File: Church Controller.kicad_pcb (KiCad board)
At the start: 2 copper layers, 50 x 90 mm, 26 parts, among them J1 Battery Connector, J2 Programming, J3 Prog Jumper, SW1 Change, SW2 Save, U1 AZ1117-3.3, U2 ESP-12E

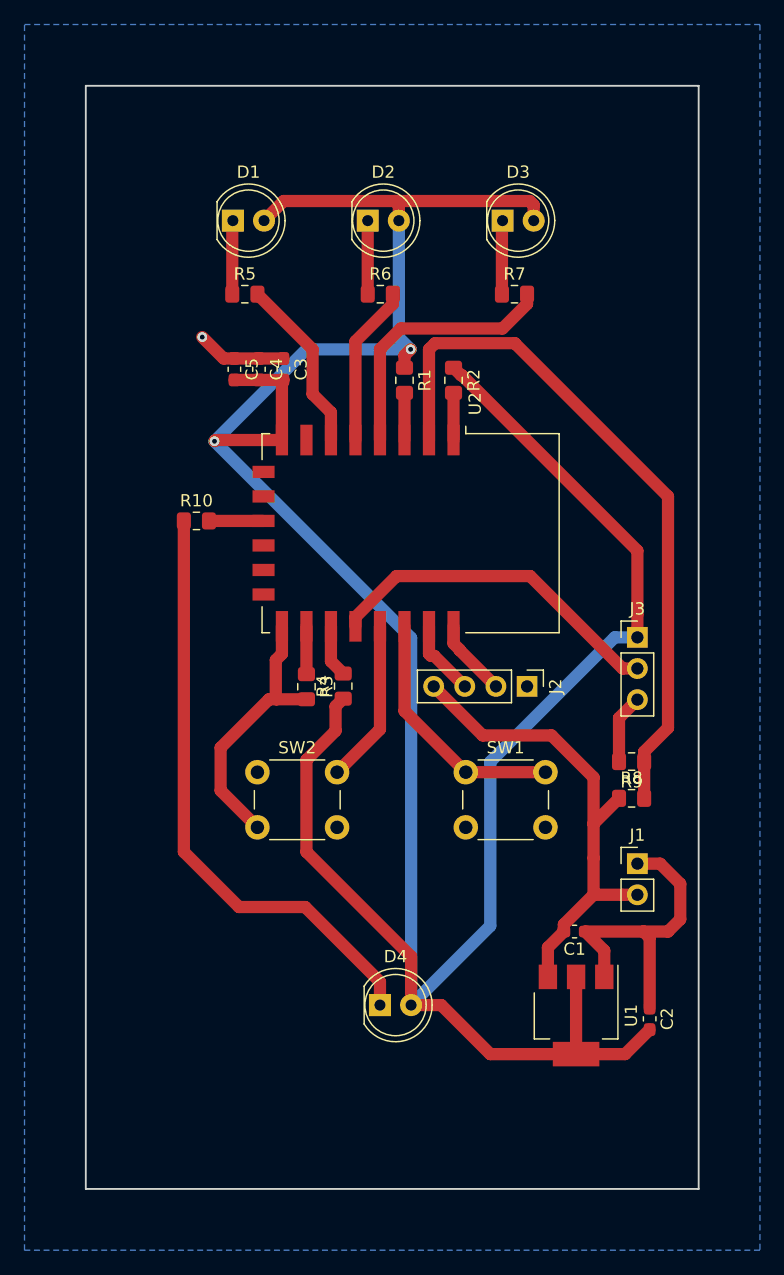
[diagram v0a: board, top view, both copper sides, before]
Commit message: Update and Corrections
Centered some misplaced components, added registration / screw holes to PCB.
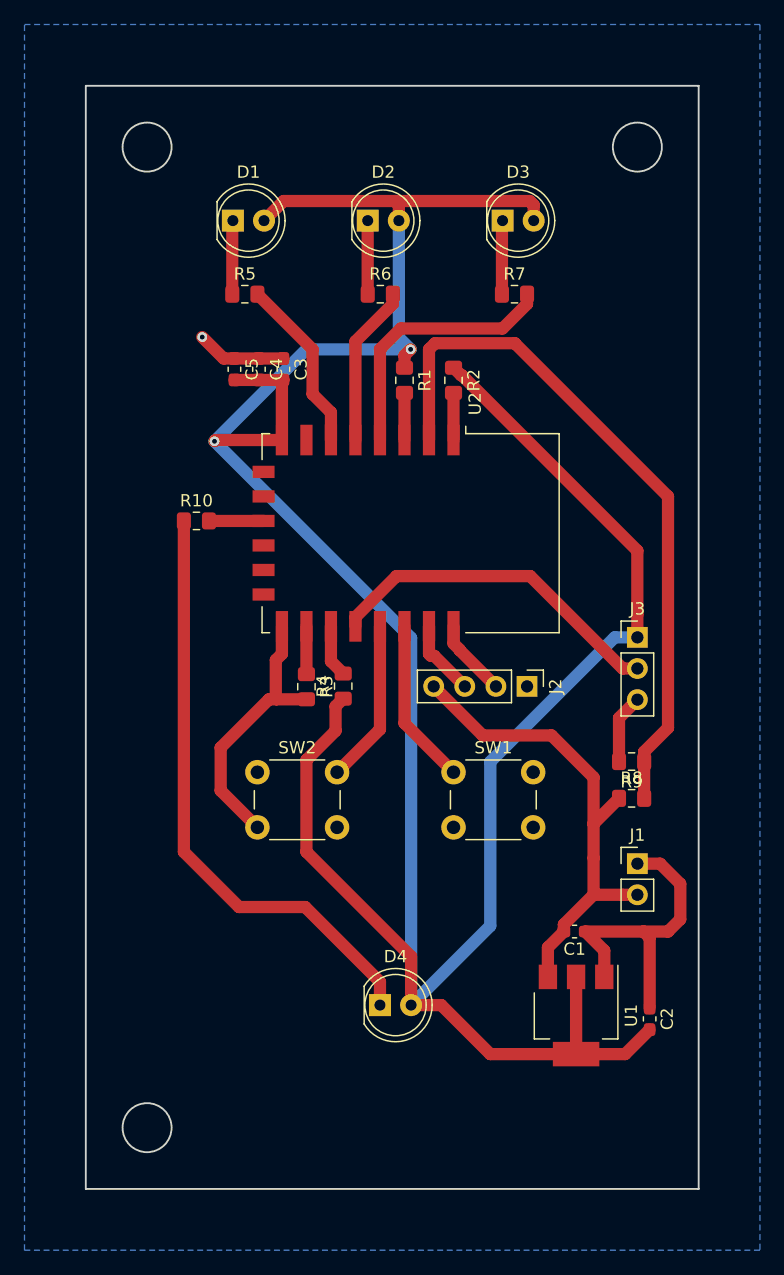
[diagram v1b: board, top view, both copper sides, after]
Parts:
- moved SW1 1.00 mm to (135.0, 106.0)
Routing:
- net /BUTTON_CHANGE: track 20.5 -> 13.6 mm
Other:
- outline, holes or cut-outs redrawn
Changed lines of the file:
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@@
   (general
     (thickness 1.6)
-    (drawings 4)
-    (tracks 136)
+    (drawings 7)
+    (tracks 135)
     (zones 0)
     (modules 26)
@@
       (drillshape 1)
       (scaleselection 1)
-      (outputdirectory ""))
+      (outputdirectory "../"))
   )
   (net 0 "")
@@
   )
   (module Button_Switch_THT:SW_PUSH_6mm_H9.5mm (layer F.Cu)
-    (at 136 106)
+    (at 135 106)
     (descr "tactile push button, 6x6mm e.g. PHAP33xx series, height=9.5mm")
     (tags "tact sw push 6mm")
@@
     )
   )
+  (gr_circle (center 110 135) (end 112 135) (layer Edge.Cuts) (width 0.15))
+  (gr_circle (center 150 55) (end 152 55) (layer Edge.Cuts) (width 0.15))
+  (gr_circle (center 110 55) (end 112 55) (layer Edge.Cuts) (width 0.15))
   (gr_line (start 105 140) (end 105 50) (layer Edge.Cuts) (width 0.15))
   (gr_line (start 155 140) (end 105 140) (layer Edge.Cuts) (width 0.15))
@@
   (segment (start 133.5 71) (end 133 71.5) (width 1) (layer F.Cu) (net 18))
   (segment (start 115.05 85.5) (end 119.5 85.5) (width 1) (layer F.Cu) (net 19))
-  (segment (start 142.5 106) (end 136 106) (width 1) (layer F.Cu) (net 20))
-  (segment (start 136 106) (end 131 101) (width 1) (layer F.Cu) (net 20))
-  (segment (start 131 101) (end 131 94.1) (width 1) (layer F.Cu) (net 20))
+  (segment (start 131 102) (end 135 106) (width 1) (layer F.Cu) (net 20))
+  (segment (start 131 94.1) (end 131 102) (width 1) (layer F.Cu) (net 20))
   (segment (start 125.5 106) (end 129 102.5) (width 1) (layer F.Cu) (net 21))
   (segment (start 129 102.5) (end 129 94.1) (width 1) (layer F.Cu) (net 21))
